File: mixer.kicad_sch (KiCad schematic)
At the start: 4 parts, among them U1 NE5532

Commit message: add gnd to audio jacks
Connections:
- net ch2_out renamed mixer_out
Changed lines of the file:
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@@
 		)
 	)
-	(hierarchical_label "ch2_out"
+	(hierarchical_label "mixer_out"
 		(shape output)
 		(at 137.16 62.23 0)

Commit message: initial component placement in pcb
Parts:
- U1: footprint NE5532DR:D8 -> NE5532DR:D8-M
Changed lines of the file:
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@@
 			)
 		)
-		(property "Footprint" "NE5532DR:D8"
+		(property "Footprint" "NE5532DR:D8-M"
 			(at 106.68 62.23 0)
 			(effects

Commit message: feat: added potentiometes footprint
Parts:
- RV1, RV2, RV3: footprint (none) -> Potentiometer_THT:Potentiometer_Alps_RK163_Single_Horizontal
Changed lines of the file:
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@@
 		(shape input)
 		(at 62.23 50.8 180)
+		(fields_autoplaced yes)
 		(effects
 			(font
@@
 		(shape output)
 		(at 137.16 62.23 0)
+		(fields_autoplaced yes)
 		(effects
 			(font
@@
 		(shape input)
 		(at 62.23 66.04 180)
+		(fields_autoplaced yes)
 		(effects
 			(font
@@
 			)
 		)
-		(property "Footprint" ""
+		(property "Footprint" "Potentiometer_THT:Potentiometer_Alps_RK163_Single_Horizontal"
 			(at 90.17 62.23 0)
 			(effects
@@
 			)
 		)
-		(property "Footprint" ""
+		(property "Footprint" "Potentiometer_THT:Potentiometer_Alps_RK163_Single_Horizontal"
 			(at 107.95 46.99 0)
 			(effects
@@
 			)
 		)
-		(property "Footprint" ""
+		(property "Footprint" "Potentiometer_THT:Potentiometer_Alps_RK163_Single_Horizontal"
 			(at 91.44 46.99 0)
 			(effects

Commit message: RAAAAH Let's gooo to production baby
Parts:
- U1: footprint NE5532DR:D8-M -> Package_DIP:DIP-8_W7.62mm_Socket
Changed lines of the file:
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@@
 		(shape input)
 		(at 62.23 50.8 180)
-		(fields_autoplaced yes)
 		(effects
 			(font
@@
 		(shape output)
 		(at 137.16 62.23 0)
-		(fields_autoplaced yes)
 		(effects
 			(font
@@
 		(shape input)
 		(at 62.23 66.04 180)
-		(fields_autoplaced yes)
 		(effects
 			(font
@@
 			)
 		)
-		(property "Footprint" "NE5532DR:D8-M"
+		(property "Footprint" "Package_DIP:DIP-8_W7.62mm_Socket"
 			(at 106.68 62.23 0)
 			(effects

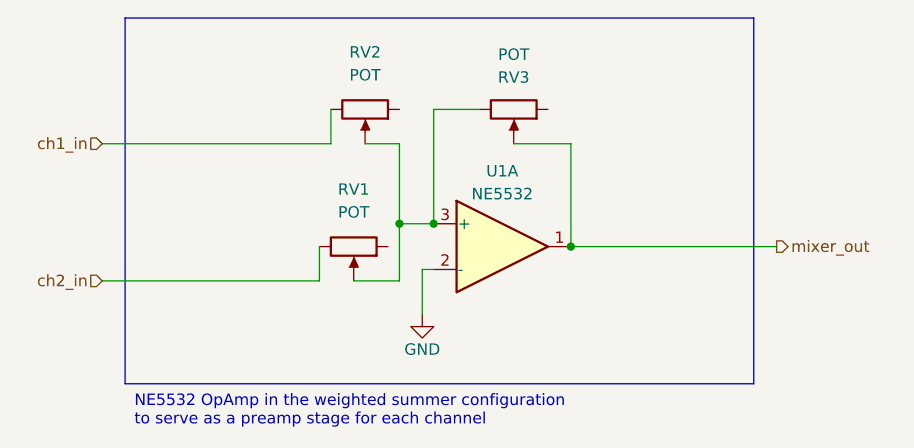
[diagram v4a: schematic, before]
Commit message: remove mask on high current tracks
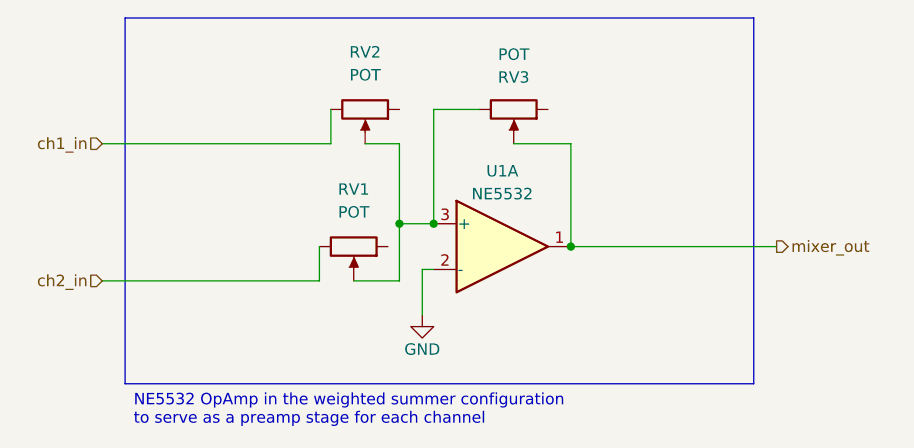
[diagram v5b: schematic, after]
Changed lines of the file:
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@@
 (kicad_sch
-	(version 20231120)
+	(version 20250114)
 	(generator "eeschema")
-	(generator_version "8.0")
+	(generator_version "9.0")
 	(paper "A5")
+	(rectangle
+		(start 64.77 36.83)
+		(end 134.62 77.47)
+		(stroke
+			(width 0)
+			(type default)
+		)
+		(fill
+			(type none)
+		)
+	)
+	(text_box "NE5532 OpAmp in the weighted summer configuration to serve as a preamp stage for each channel\n"
+		(exclude_from_sim no)
+		(at 64.77 77.47 0)
+		(size 57.15 8.89)
+		(margins 0.9524 0.9524 0.9524 0.9524)
+		(stroke
+			(width -0.0001)
+			(type default)
+		)
+		(fill
+			(type none)
+		)
+		(effects
+			(font
+				(size 1.27 1.27)
+			)
+			(justify left top)
+		)
+	)
 	(junction
 		(at 114.3 62.23)
@@
 		)
 	)
-	(rectangle
-		(start 64.77 36.83)
-		(end 134.62 77.47)
-		(stroke
-			(width 0)
-			(type default)
-		)
-		(fill
-			(type none)
-		)
-	)
-	(text_box "NE5532 OpAmp in the weighted summer configuration to serve as a preamp stage for each channel\n"
-		(exclude_from_sim no)
-		(at 64.77 77.47 0)
-		(size 57.15 8.89)
-		(stroke
-			(width -0.0001)
-			(type default)
-		)
-		(fill
-			(type none)
-		)
-		(effects
-			(font
-				(size 1.27 1.27)
-			)
-			(justify left top)
-		)
-	)
